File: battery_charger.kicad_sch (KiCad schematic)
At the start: 83 parts, among them J2 Barrel_Jack_Switch_Pin3Ring, Q3 SS8050, Q4 SS8050, U4 TP5100, U5 LM2596S-buck

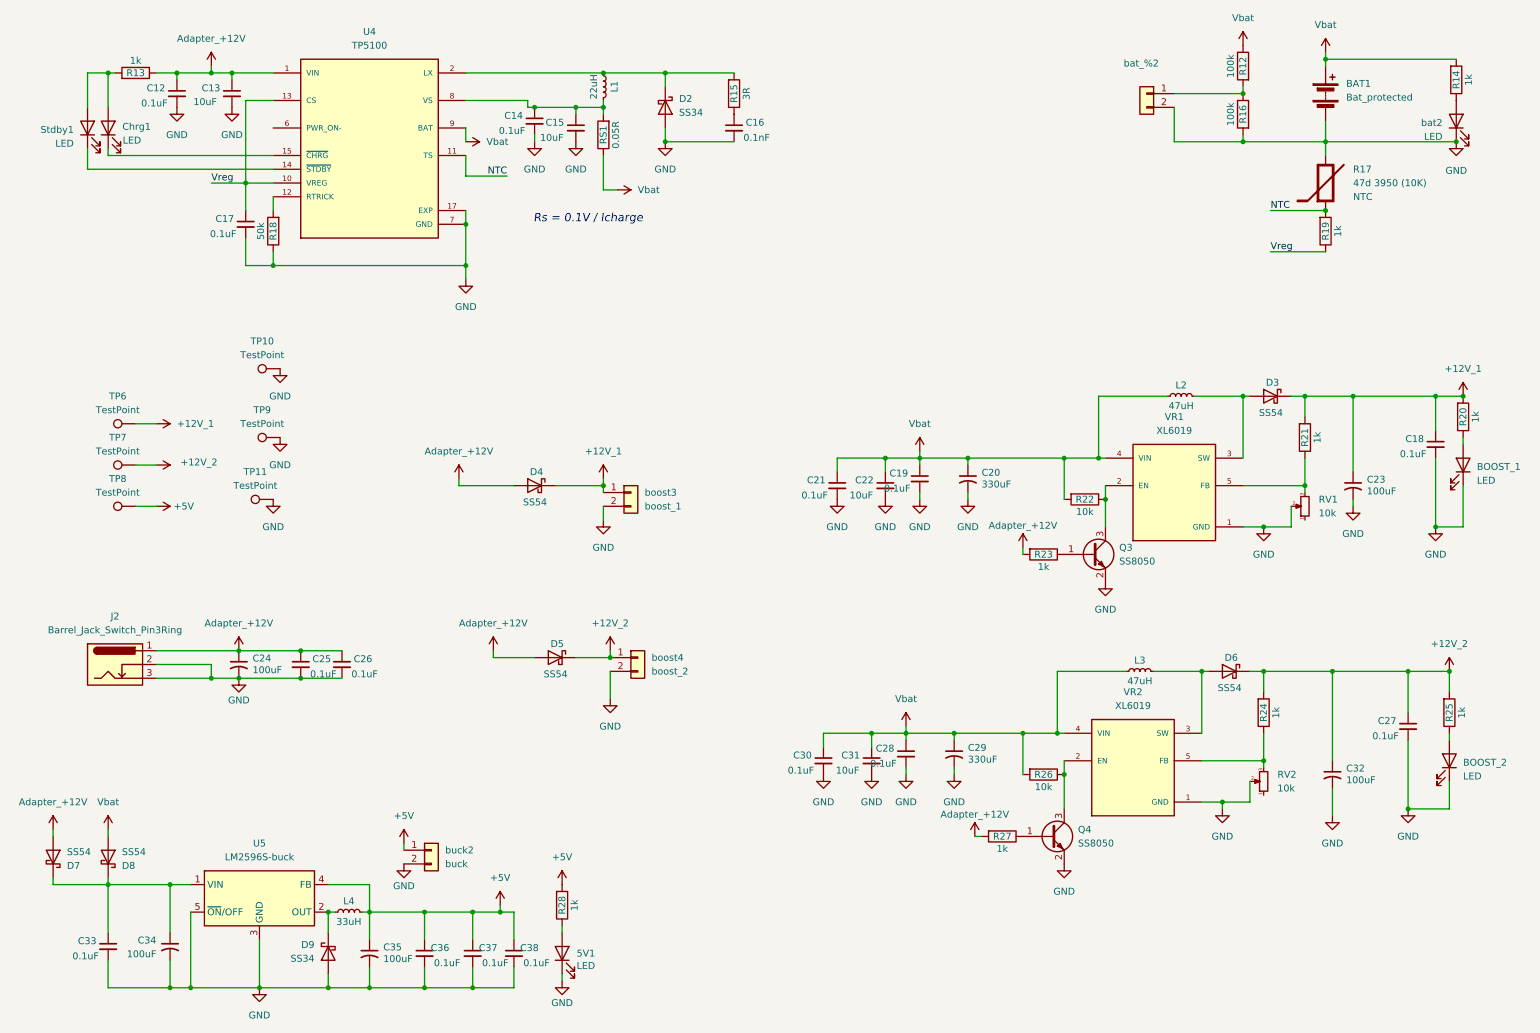
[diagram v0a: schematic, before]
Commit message: made into blocks
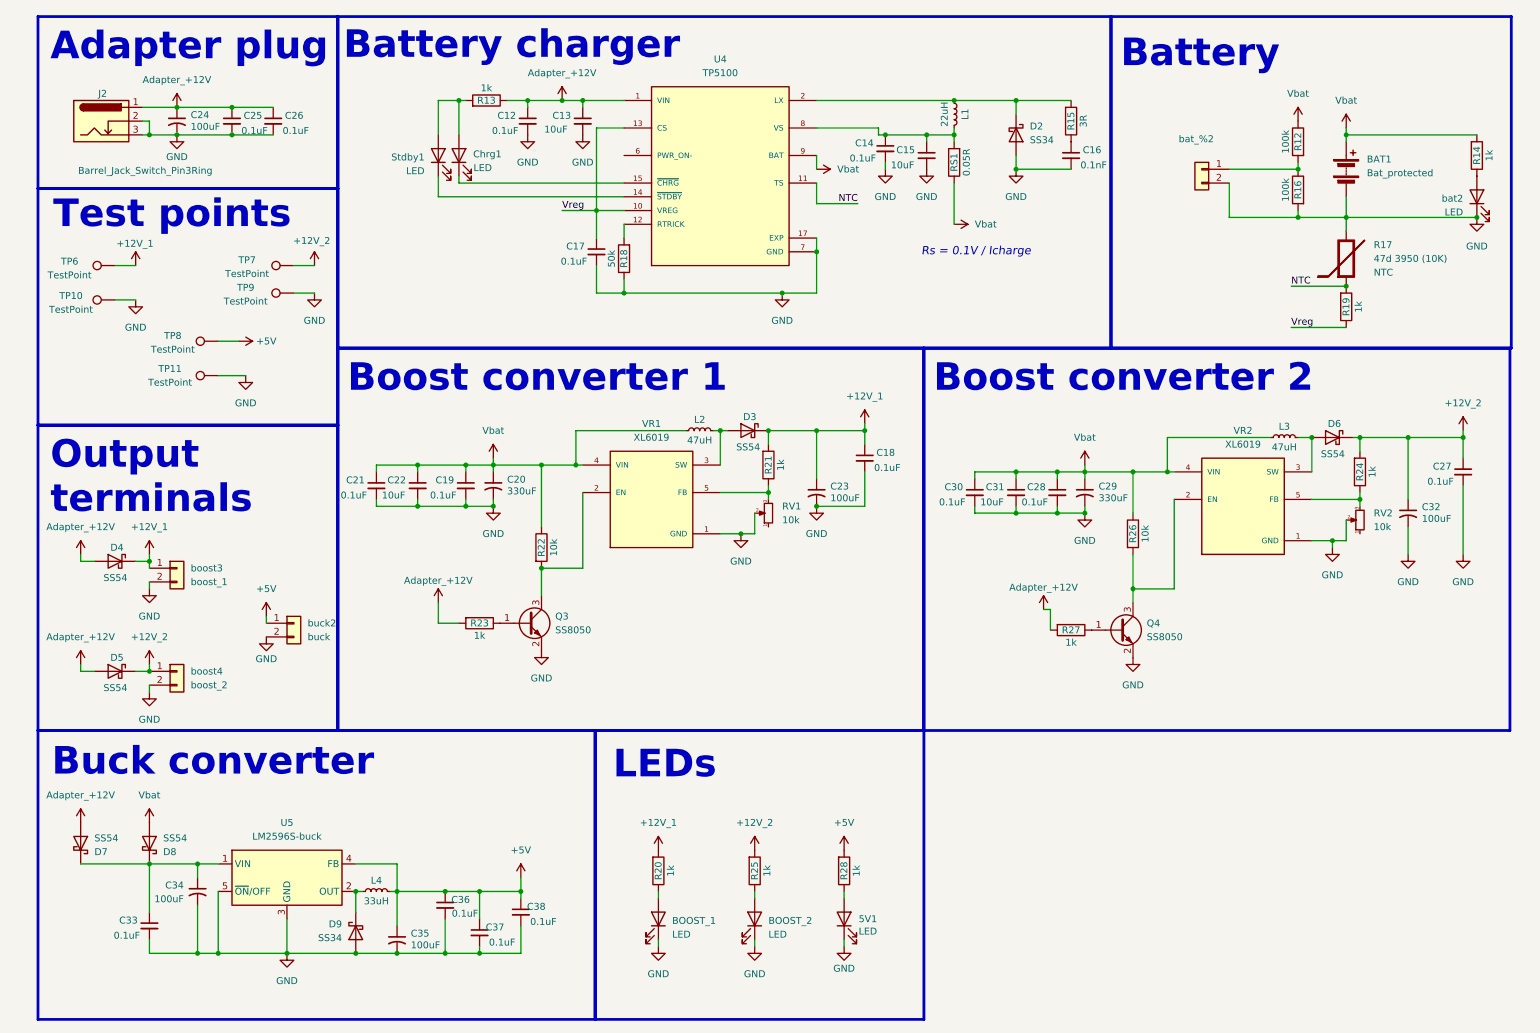
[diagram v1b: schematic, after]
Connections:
- net Vbat: now also R22.1, R26.1; no longer R22.2, R26.2
- net at Q3.3 (C), VR1.2 (EN): now also R22.2; no longer R22.1
- net at Q4.3 (C), VR2.2 (EN): now also R26.2; no longer R26.1
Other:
- note added: "Adapter plug"
- note added: "Battery"
- note added: "Battery charger"
- note added: "Boost converter 1"
- note added: "Boost converter 2"
- note added: "Buck converter"
- note added: "LEDs"
- note added: "Output terminals"
- note added: "Test points"
- moved on the sheet: 5V1, BAT1, BOOST_1, BOOST_2, C12, C13, C14, C15, C16, C17, C18, C19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

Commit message: Update - 22-Feb-26
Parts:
- R12: value 100k -> 150k
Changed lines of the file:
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@@
 			)
 		)
-		(property "Value" "100k"
+		(property "Value" "150k"
 			(at 242.824 35.56 90)
 			(effects

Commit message: added power button
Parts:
- removed C21, C28, C30: 0.1uF, PCM_4ms_Capacitor:C_0603, symbol Device:C_Small
- removed C22, C31: 10uF, PCM_4ms_Capacitor:C_0603, symbol Device:C_Small
- removed U5: LM2596S-buck, PCM_Package_TO_SOT_SMD_AKL:TO-263-5_TabPin3_ThermalVias, symbol Regulator_Switching:LM2596S-5
- added D9: SS34, Diode_SMD:D_SMA, symbol Diode:1N5822
- added R29: 2k, PCM_4ms_Resistor:R_0603, symbol Device:R
- added RV3: 10k, PCM_Potentiometer_THT_AKL_Double:Potentiometer_Bourns_3266Y_Vertical, symbol Device:R_Potentiometer_Small
- added U5: XL4015, Package_TO_SOT_SMD:TO-263-5_TabPin3, symbol Regulator_Switching:XL4015
- added power_button1: pb, TerminalBlock_TE-Connectivity:TerminalBlock_TE_282834-2_1x02_P2.54mm_Horizontal, symbol PCM_4ms_Connector:Conn_01x02
- BAT1: footprint Connector_JST:JST_VH_B2P-VH-B_1x02_P3.96mm_Vertical -> TerminalBlock_TE-Connectivity:TerminalBlock_TE_282834-2_1x02_P2.54mm_Horizontal
- renumbered C24 to C12, C25 to C13, C26 to C14, C12 to C15, C13 to C16, C14 to C17, C15 to C18, C16 to C19, C17 to C20, C18 to C21, C27 to C22, C19 to C23, C20 to C24, C23 to C25, C29 to C26, C32 to C27, C34 to C28, C36 to C29, C33 to C30, C38 to C31, C37 to C32, C35 to C33, D9 to D10, D6 to D4, D4 to D5, D5 to D6, R13 to R12, R15 to R13, R12 to R14, R14 to R15, R18 to R17, R17 to R18, R21 to R20, R24 to R21, R26 to R22, R22 to R23, R23 to R24, R27 to R25, R20 to R26, R25 to R27, TP6 to TP4, TP7 to TP5, TP9 to TP6, TP10 to TP7, TP11 to TP9
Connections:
- net +5V: now also D9.1 (K); no longer C29.1, C31.1, C32.1, C33.1, L4.2
- net GND: now also R29.1, U5.1 (GND), power_button1.2 (Pin_2); no longer BAT1.2 (-), C12.2, C13.2, C14.2, C15.2, C16.2, C17.2, C18.2, C19.2, C20.2, D2.2 (A), J2.2, J2.3, R17.1, R18.1 (+), U4.17 (EXP), U4.7 (GND)
- net at C28.1, C30.1, D7.1 (K)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: now also U5.4 (VC), U5.5 (VIN)
- net at D10.1 (K), L4.1: now also U5.3 (SW)
- new net: C29.1, C31.1, C32.1, C33.1, D9.2 (A), L4.2, RV3.1
- new net Earth: BAT1.2 (-), C12.2, C13.2, C14.2, C15.2, C16.2, C17.2, C18.2, C19.2, C20.2, D2.2 (A), J2.2, J2.3, R17.1, R18.1 (+), U4.17 (EXP), U4.7 (GND), power_button1.1 (Pin_1)
- new net FB: R29.2, RV3.2, U5.2 (FB)
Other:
- moved on the sheet: C29, C31, C32, C33, D10, D7, L4

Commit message: changed silk screen, added grid for star ground
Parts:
- J2: footprint my_custom_footprint:GCT_DCJ200-10-A-XX-K_REVA -> Connector_BarrelJack:BarrelJack_GCT_DCJ200-10-A_Horizontal
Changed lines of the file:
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@@
 			)
 		)
-		(property "Footprint" "my_custom_footprint:GCT_DCJ200-10-A-XX-K_REVA"
+		(property "Footprint" "Connector_BarrelJack:BarrelJack_GCT_DCJ200-10-A_Horizontal"
 			(at 25.4 32.766 0)
 			(effects
